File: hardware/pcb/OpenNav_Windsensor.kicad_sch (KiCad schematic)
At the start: 9 parts, among them IC1 AS5600-ASOT, J1 Conn_01x02_Pin, U1 XIAO-ESP32-C6, U2 StpDwnE3.3-0.5, U3 SS411P, U4 DS18B20

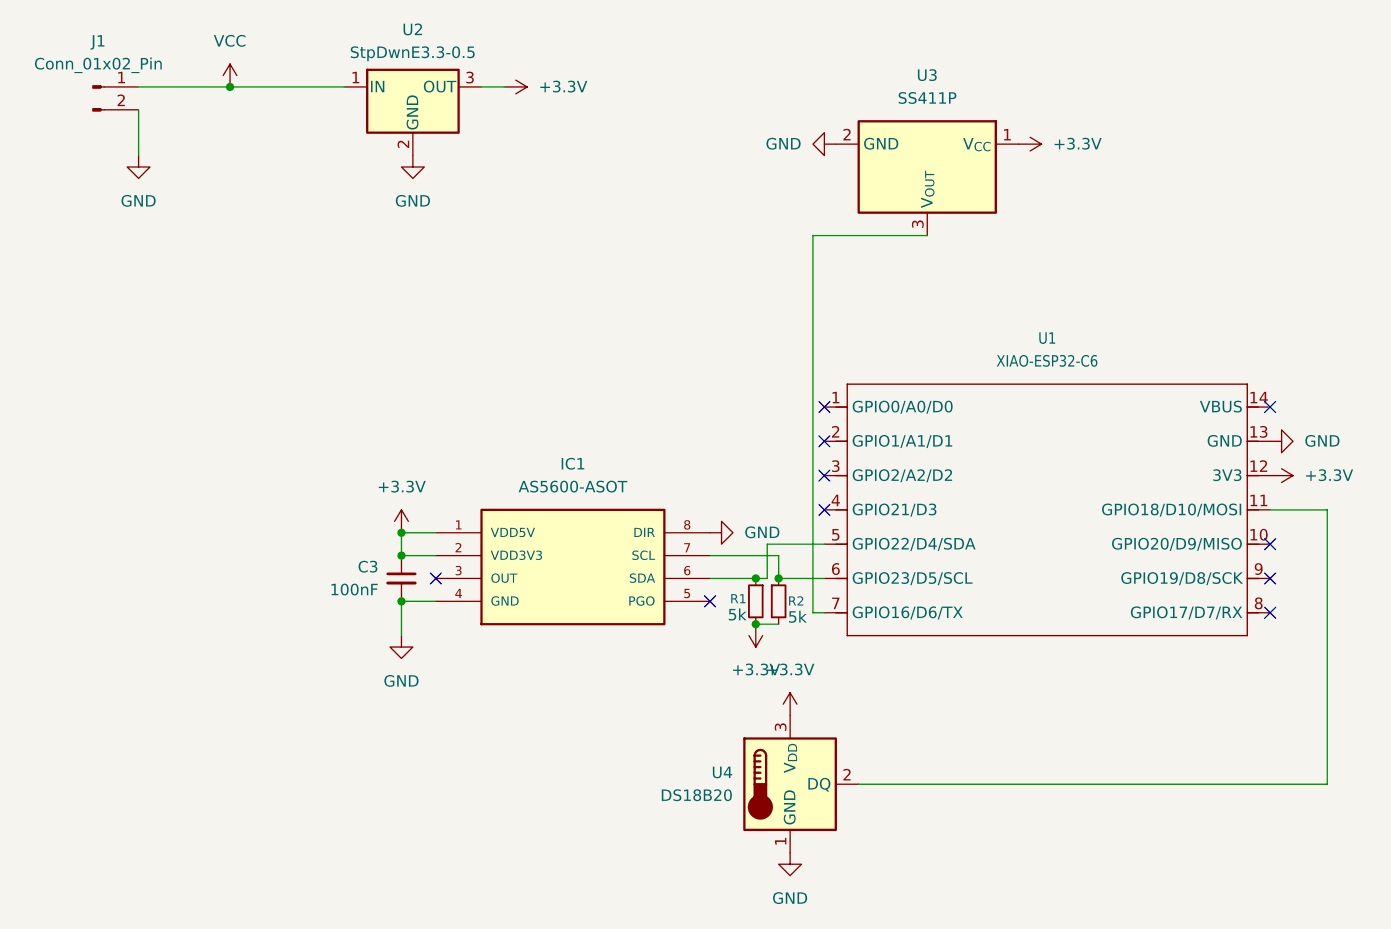
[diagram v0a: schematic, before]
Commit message: Added software, corrected for ESP32C6 (untested)
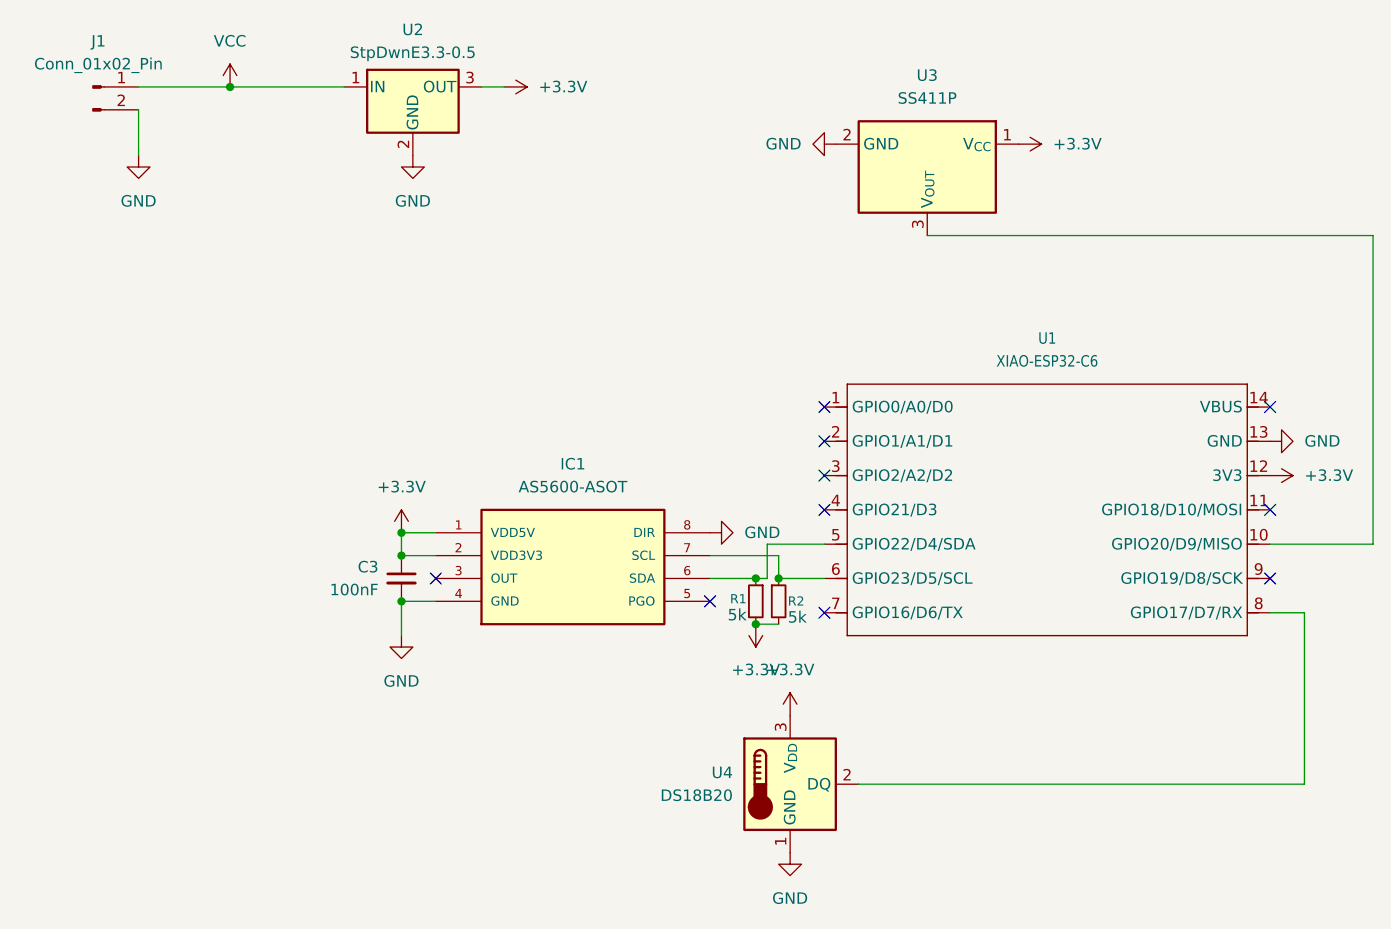
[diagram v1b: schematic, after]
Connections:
- net at U1.10 (GPIO20/D9/MISO): now also U3.3 (V_{OUT})
- net at U1.11 (GPIO18/D10/MOSI): no longer U4.2 (DQ)
- net at U1.7 (GPIO16/D6/TX): no longer U3.3 (V_{OUT})
- net at U1.8 (GPIO17/D7/RX): now also U4.2 (DQ)
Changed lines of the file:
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@@
 	)
 	(no_connect
-		(at 175.26 127)
+		(at 175.26 115.57)
 	)
 	(no_connect
@@
 	)
 	(no_connect
-		(at 175.26 119.38)
+		(at 125.73 127)
 	)
 	(no_connect
@@
 	(wire
 		(pts
+			(xy 186.69 119.38) (xy 175.26 119.38)
+		)
+		(stroke
+			(width 0)
+			(type default)
+		)
+	)
+	(wire
+		(pts
 			(xy 59.69 68.58) (xy 72.39 68.58)
+		)
+		(stroke
+			(width 0)
+			(type default)
+		)
+	)
+	(wire
+		(pts
+			(xy 179.07 127) (xy 175.26 127)
 		)
 		(stroke
@@
 	(wire
 		(pts
-			(xy 124.46 127) (xy 125.73 127)
-		)
-		(stroke
-			(width 0)
-			(type default)
-		)
-	)
-	(wire
-		(pts
 			(xy 78.74 125.73) (xy 78.74 129.54)
 		)
@@
 		(pts
 			(xy 119.38 119.38) (xy 125.73 119.38)
+		)
+		(stroke
+			(width 0)
+			(type default)
+		)
+	)
+	(wire
+		(pts
+			(xy 137.16 85.09) (xy 186.69 85.09)
 		)
 		(stroke
@@
 	(wire
 		(pts
-			(xy 129.54 146.05) (xy 181.61 146.05)
+			(xy 129.54 146.05) (xy 179.07 146.05)
 		)
 		(stroke
@@
 	(wire
 		(pts
-			(xy 181.61 146.05) (xy 181.61 115.57)
+			(xy 179.07 146.05) (xy 179.07 127)
 		)
 		(stroke
@@
 	(wire
 		(pts
-			(xy 124.46 85.09) (xy 137.16 85.09)
+			(xy 186.69 85.09) (xy 186.69 119.38)
 		)
 		(stroke
-			(width 0)
-			(type default)
-		)
-	)
-	(wire
-		(pts
-			(xy 124.46 85.09) (xy 124.46 127)
-		)
-		(stroke
-			(width 0)
-			(type default)
-		)
-	)
-	(wire
-		(pts
-			(xy 181.61 115.57) (xy 175.26 115.57)
-		)
-		(stroke

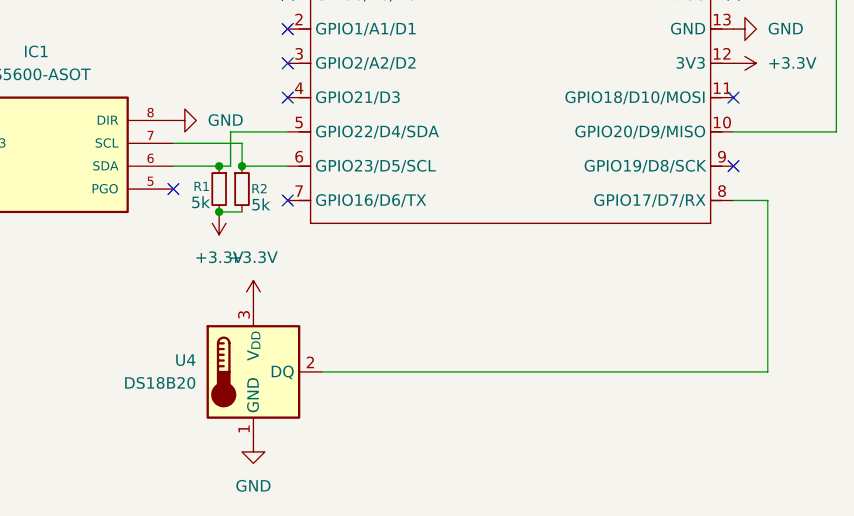
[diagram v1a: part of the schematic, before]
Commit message: Corrected temperature sensor bug
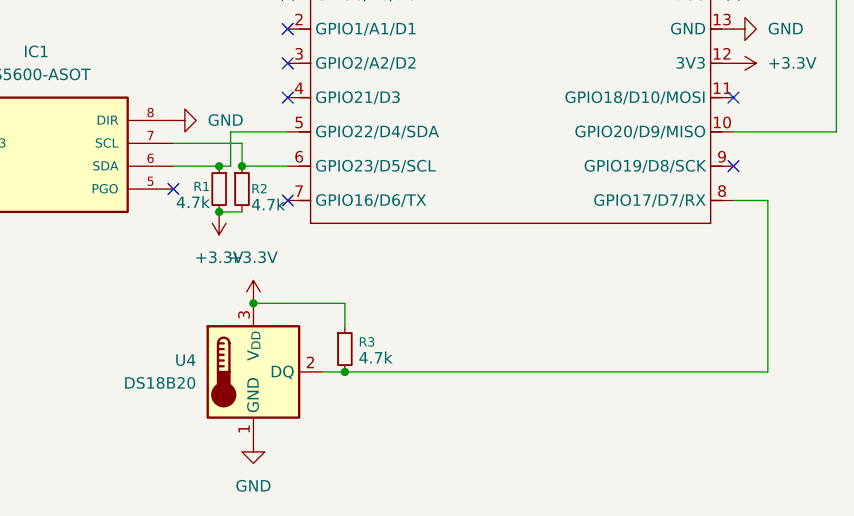
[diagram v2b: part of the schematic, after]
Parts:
- added R3: 4.7k, Resistor_SMD:R_1206_3216Metric_Pad1.30x1.75mm_HandSolder, symbol Device:R_Small
- R1, R2: value 5k -> 4.7k
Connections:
- net +3.3V: now also R3.1
- net at U1.8 (GPIO17/D7/RX), U4.2 (DQ): now also R3.2
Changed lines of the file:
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@@
+	)
+	(junction
+		(at 132.08 146.05)
+		(diameter 0)
+		(color 0 0 0 0)
 	)
 	(junction
@@
 	)
 	(junction
+		(at 121.92 138.43)
+		(diameter 0)
+		(color 0 0 0 0)
+	)
+	(junction
 		(at 78.74 125.73)
 		(diameter 0)
@@
 	(wire
 		(pts
+			(xy 132.08 140.97) (xy 132.08 138.43)
+		)
+		(stroke
+			(width 0)
+			(type default)
+		)
+	)
+	(wire
+		(pts
 			(xy 186.69 119.38) (xy 175.26 119.38)
 		)
@@
 	(wire
 		(pts
+			(xy 132.08 138.43) (xy 121.92 138.43)
+		)
+		(stroke
+			(width 0)
+			(type default)
+		)
+	)
+	(wire
+		(pts
 			(xy 49.53 71.12) (xy 49.53 76.2)
 		)
@@
 	(wire
 		(pts
+			(xy 132.08 146.05) (xy 179.07 146.05)
+		)
+		(stroke
+			(width 0)
+			(type default)
+		)
+	)
+	(wire
+		(pts
 			(xy 113.03 123.19) (xy 118.11 123.19)
 		)
@@
 	(wire
 		(pts
-			(xy 129.54 146.05) (xy 179.07 146.05)
+			(xy 129.54 146.05) (xy 132.08 146.05)
 		)
 		(stroke
@@
 			)
 		)
-		(property "Value" "5k"
+		(property "Value" "4.7k"
 			(at 121.666 127.508 0)
 			(effects
@@
 	)
 	(symbol
+		(lib_id "Device:R_Small")
+		(at 132.08 143.51 0)
+		(unit 1)
+		(exclude_from_sim no)
+		(in_bom yes)
+		(on_board yes)
+		(dnp no)
+		(property "Reference" "R3"
+			(at 133.604 142.748 0)
+			(effects
+				(font
+					(size 1.016 1.016)
+				)
+				(justify left)
+			)
+		)
+		(property "Value" "4.7k"
+			(at 133.604 144.526 0)
+			(effects
+				(font
+					(size 1.27 1.27)
+				)
+				(justify left)
+			)
+		)
+		(property "Footprint" "Resistor_SMD:R_1206_3216Metric_Pad1.30x1.75mm_HandSolder"
+			(at 132.08 143.51 0)
+			(effects
+				(font
+					(size 1.27 1.27)
+				)
+				(hide yes)
+			)
+		)
+		(property "Datasheet" "~"
+			(at 132.08 143.51 0)
+			(effects
+				(font
+					(size 1.27 1.27)
+				)
+				(hide yes)
+			)
+		)
+		(property "Description" "Resistor, small symbol"
+			(at 132.08 143.51 0)
+			(effects
+				(font
+					(size 1.27 1.27)
+				)
+				(hide yes)
+			)
+		)
+		(pin "2"
+		)
+		(pin "1"
+		)
+		(instances
+			(project "OpenNav_Windsensor"
+				(path "/a81e5ad1-b2a3-4a64-8503-427321b39e31"
+					(reference "R3")
+					(unit 1)
+				)
+			)
+		)
+	)
+	(symbol
 		(lib_id "power:VCC")
 		(at 59.69 68.58 0)
@@
 			)
 		)
-		(property "Value" "5k"
+		(property "Value" "4.7k"
 			(at 117.094 127.254 0)
 			(effects
